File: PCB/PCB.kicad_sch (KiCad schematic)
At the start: 14 parts

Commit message: resized and gerber
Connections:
- net GND: no longer PicoL1.18 (Pin_18), PicoL1.3 (Pin_3), PicoL1.8 (Pin_8), PicoR1.13 (Pin_13), PicoR1.18 (Pin_18), PicoR1.3 (Pin_3), PicoR1.8 (Pin_8), QTR-8RC1.11 (Pin_11), TB6612FNGL1.1 (Pin_1), TB6612FNGR1.3 (Pin_3), TB6612FNGR1.8 (Pin_8)
- new net GND18: PicoL1.18 (Pin_18), TB6612FNGR1.3 (Pin_3)
- new net GND3: PicoL1.3 (Pin_3), QTR-8RC1.11 (Pin_11)

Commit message: 100x100
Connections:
- net GND: now also PicoR1.18 (Pin_18); no longer PicoL1.13 (Pin_13)
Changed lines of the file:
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@@
 	(symbol
 		(lib_id "power:GND")
-		(at 60.96 102.87 270)
+		(at 87.63 77.47 90)
 		(unit 1)
 		(exclude_from_sim no)
@@
 		(dnp no)
 		(property "Reference" "#PWR015"
-			(at 54.61 102.87 0)
+			(at 93.98 77.47 0)
 			(effects
 				(font
@@
 		)
 		(property "Value" "GND"
-			(at 54.356 103.124 90)
+			(at 94.234 77.216 90)
 			(effects
 				(font
@@
 		)
 		(property "Footprint" ""
-			(at 60.96 102.87 0)
+			(at 87.63 77.47 0)
 			(effects
 				(font
@@
 		)
 		(property "Datasheet" ""
-			(at 60.96 102.87 0)
+			(at 87.63 77.47 0)
 			(effects
 				(font
@@
 		)
 		(property "Description" "Power symbol creates a global label with name \"GND\" , ground"
-			(at 60.96 102.87 0)
+			(at 87.63 77.47 0)
 			(effects
 				(font

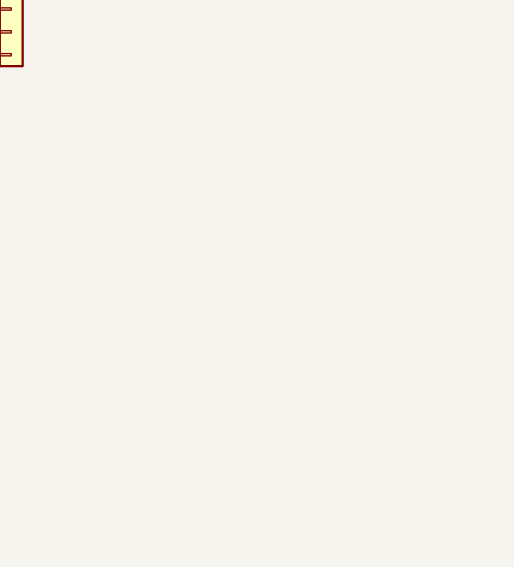
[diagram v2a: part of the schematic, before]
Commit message: screw holes
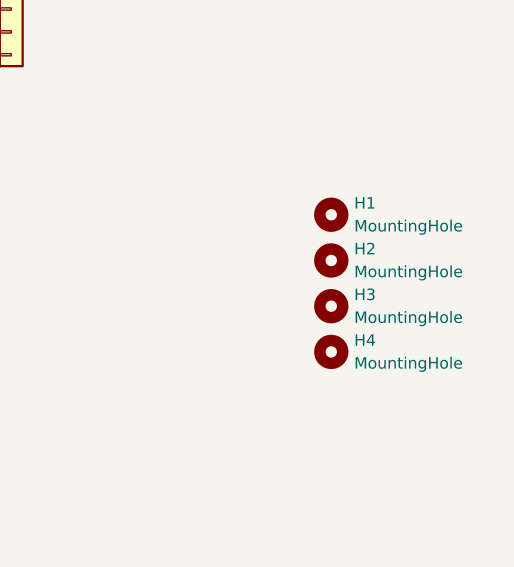
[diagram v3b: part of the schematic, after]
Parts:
- added H1, H2, H3, H4: MountingHole, MountingHole:MountingHole_3.2mm_M3, symbol Mechanical:MountingHole
